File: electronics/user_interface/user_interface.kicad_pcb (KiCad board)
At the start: 2 copper layers, 100 x 100 mm, 66 parts, among them J1 Conn_01x06, J2 Conn_02x05_Odd_Even, SW1 ALPS_EC11E18244A5, U1 PCF8574, U2 PCF8574

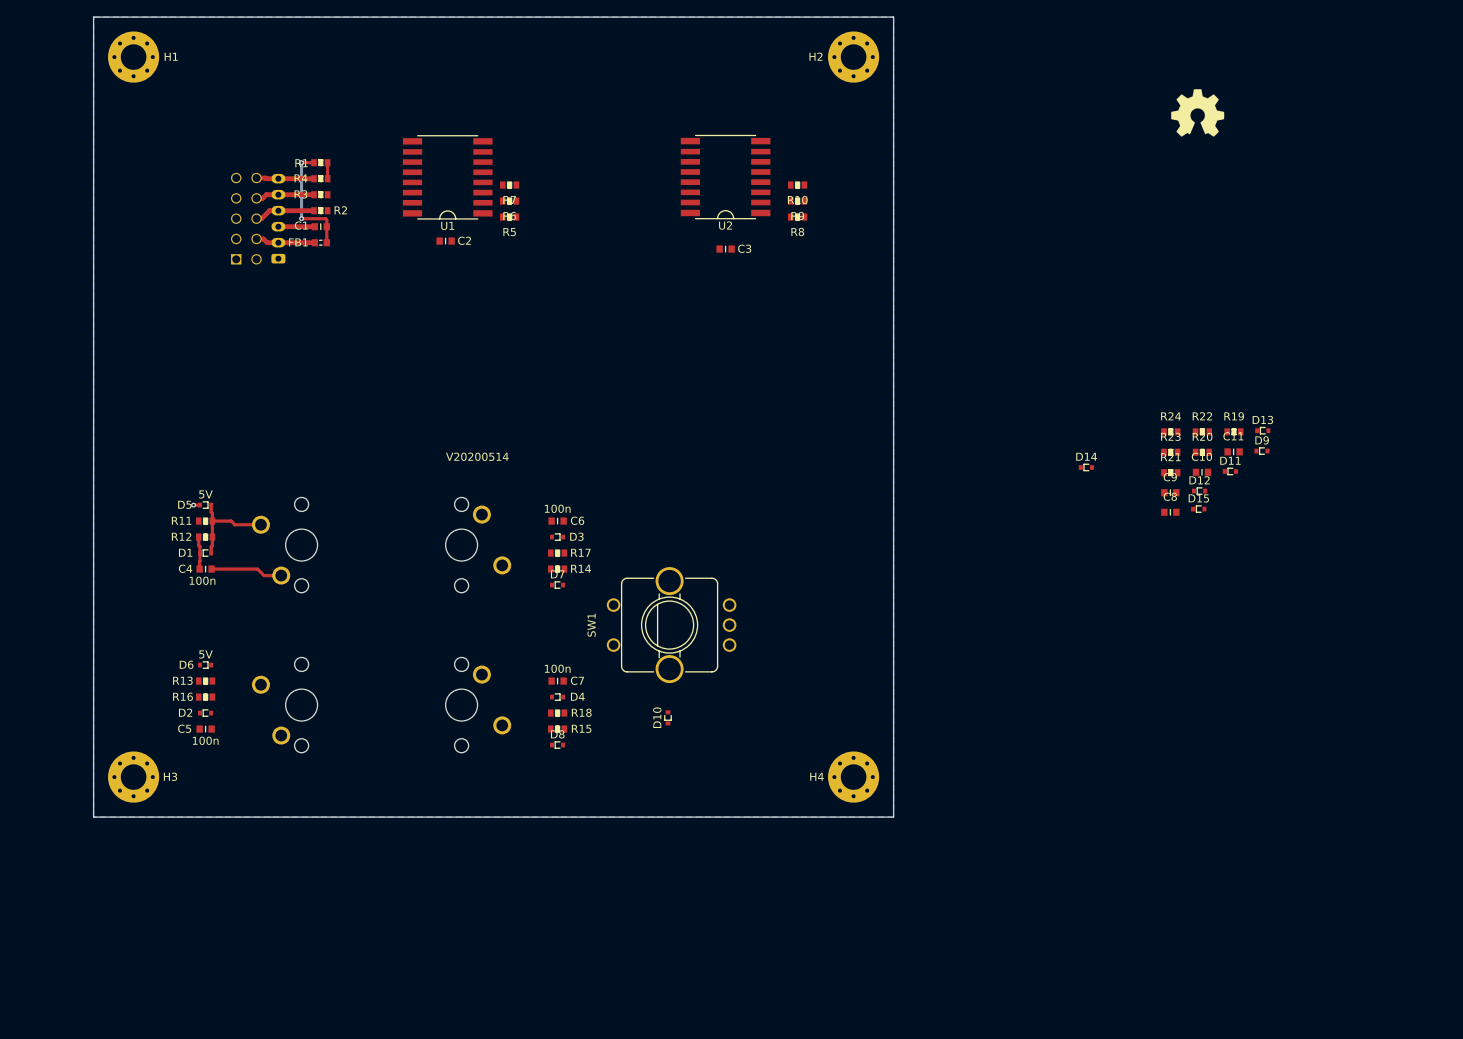
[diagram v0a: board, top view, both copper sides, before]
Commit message: imported LCD parts, changed board size
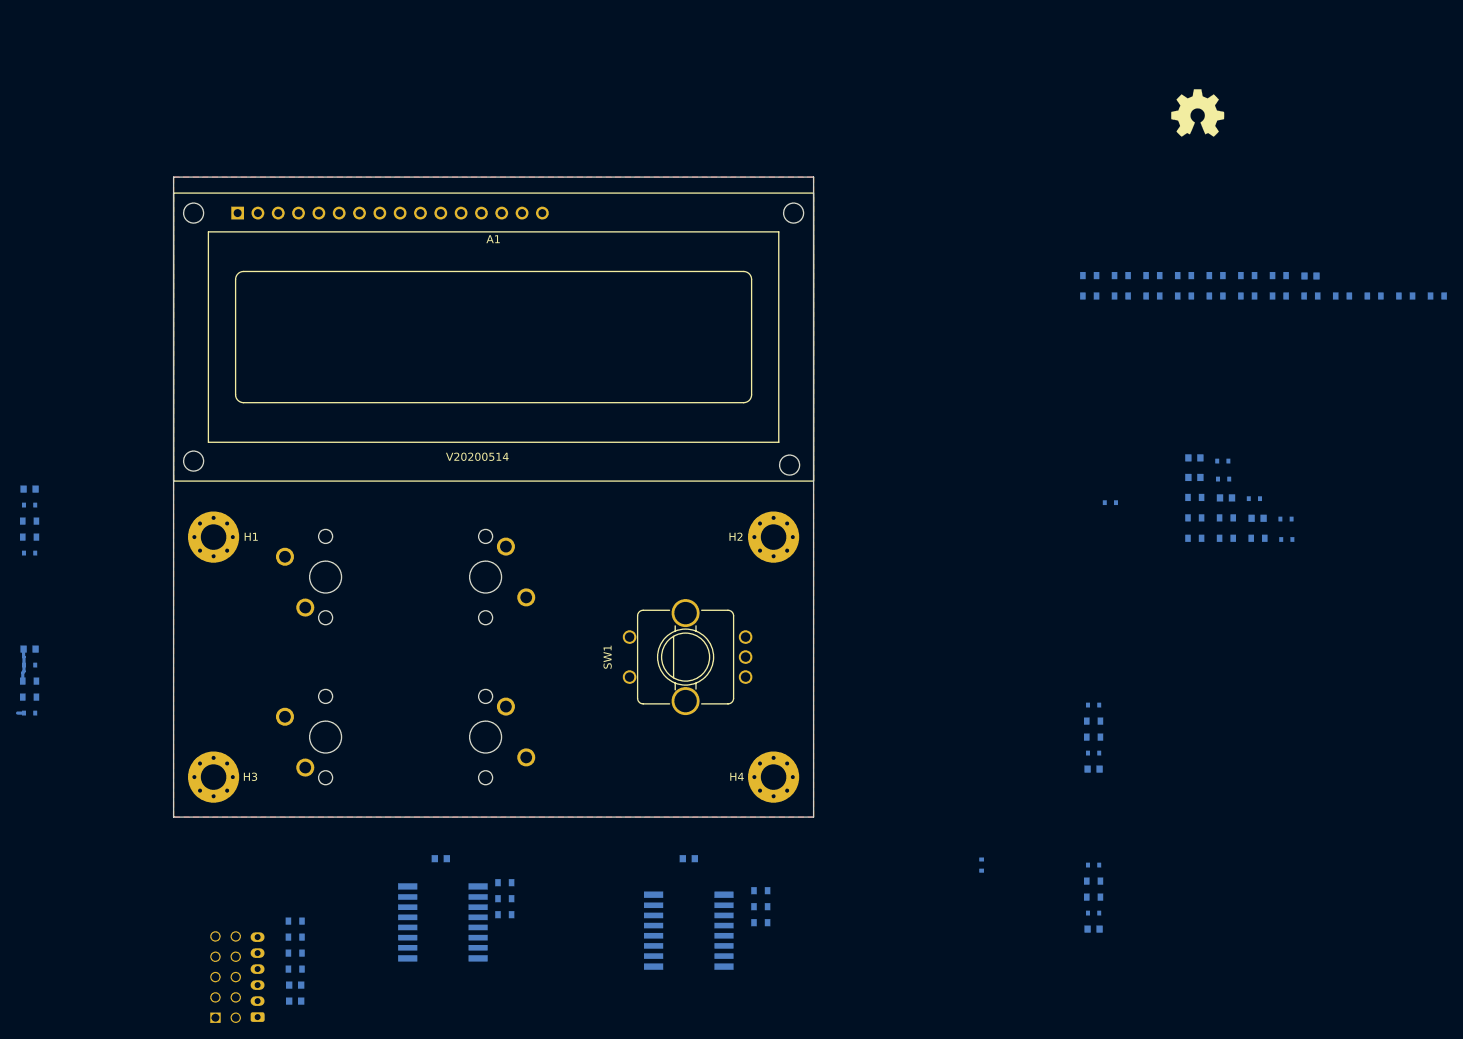
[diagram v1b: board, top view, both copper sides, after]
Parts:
- added A1: LCM1602, SquantorModules:LCM1602K, F.Cu at (150.0, 90.0)
- added C12: 1u, SquantorRcl:C_0603, B.Cu at (252.1, 82.4)
- added R25: 4.7K, SquantorRcl:R_0603_hand, B.Cu at (228.5, 84.9)
- added R26: 4.7K, SquantorRcl:R_0603_hand, B.Cu at (232.4, 84.9)
- added R27: 4.7K, SquantorRcl:R_0603_hand, B.Cu at (236.4, 84.9)
- added R28: 4.7K, SquantorRcl:R_0603_hand, B.Cu at (240.3, 84.9)
- added R29: 4.7K, SquantorRcl:R_0603_hand, B.Cu at (244.3, 84.9)
- added R30: 4.7K, SquantorRcl:R_0603_hand, B.Cu at (248.2, 84.9)
- added R31: 4.7K, SquantorRcl:R_0603_hand, B.Cu at (252.2, 84.9)
- added R32: 4.7K, SquantorRcl:R_0603_hand, B.Cu at (256.1, 84.9)
- added R33: 4.7K, SquantorRcl:R_0603_hand, B.Cu at (248.2, 82.3)
- added R34: 4.7K, SquantorRcl:R_0603_hand, B.Cu at (260.1, 84.9)
- added R35: 4.7K, SquantorRcl:R_0603_hand, B.Cu at (264.0, 84.9)
- added R36: 4.7K, SquantorRcl:R_0603_hand, B.Cu at (268.0, 84.9)
- added R37: 4.7K, SquantorRcl:R_0603_hand, B.Cu at (224.5, 82.3)
- added R38: TBD, SquantorRcl:R_0603_hand, B.Cu at (228.5, 82.3)
- added R39: 0, SquantorRcl:R_0603_hand, B.Cu at (232.4, 82.3)
- added R40: TBD, SquantorRcl:R_0603_hand, B.Cu at (236.4, 82.3)
- added R41: TBD, SquantorRcl:R_0603_hand, B.Cu at (240.3, 82.3)
- added R42: 0, SquantorRcl:R_0603_hand, B.Cu at (244.3, 82.3)
- added R43: NTC?, SquantorRcl:R_0603_hand, B.Cu at (224.5, 84.9)
- C1, C10, C11, C2, C3, C4, C5, C6, C7, C8, C9, D1, D10, D11, D12, D13, D14, D15, D2, D3, D4, D5, D6, D7, D8, D9, FB1, R1, R10, R11, R12, R13, R14, R15, R16, R17, R18, R19, R2, R20, R21, R22, R23, R24, R3, R4, R5, R6, R7, R8, R9, U1, U2: moved to B.Cu
- moved C1 94.9 mm to (125.2, 171.0)
- moved FB1 94.9 mm to (125.2, 173.0)
- moved R1 94.9 mm to (125.2, 163.0)
- moved R2 94.9 mm to (125.2, 169.0)
- moved R3 94.9 mm to (125.2, 167.0)
- moved R4 94.9 mm to (125.2, 165.0)
- moved J1 94.8 mm to (120.5, 175.0)
- moved J2 94.8 mm to (116.5, 170.0)
- moved U2 94.3 mm to (174.4, 164.2)
- moved U1 93.1 mm to (143.7, 163.2)
- moved R10 92.3 mm to (183.4, 163.2)
- moved R7 91.2 mm to (151.4, 162.2)
- moved R9 88.3 mm to (183.4, 161.2)
- moved R6 87.2 mm to (151.4, 160.2)
- moved R8 84.3 mm to (183.4, 159.2)
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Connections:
- U1 pad 10: Net-(U1-Pad10) -> /RW
- U1 pad 11: Net-(U1-Pad11) -> /RS
- U1 pad 4: Net-(U1-Pad4) -> /DB0
- U1 pad 5: Net-(U1-Pad5) -> /DB1
- U1 pad 6: Net-(U1-Pad6) -> /DB2
- U1 pad 7: Net-(U1-Pad7) -> /DB3
- U1 pad 9: Net-(U1-Pad9) -> /E
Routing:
- net /VDD: track 14.6 -> 0.00 mm, vias 2 -> 0
- net /VSS: track 14.4 -> 0.80 mm, vias 1 -> 0
- net Net-(D1-Pad2): track 12.4 -> 0.00 mm
- net /SDA_RAW: track 7.59 -> 0.00 mm
- net /VDD_RAW: track 7.47 -> 0.00 mm
- net /SCL_RAW: track 7.37 -> 0.00 mm
- net /!INT_RAW: track 7.21 -> 0.00 mm
- net /!INT: track 2.00 -> 0.00 mm
- added copper zone on F.Cu, net /VSS
- removed copper zone on B.Cu, net /VSS
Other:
- board size 100 x 100 mm -> 80 x 80 mm

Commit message: beautified schematic a bit, passes ERC
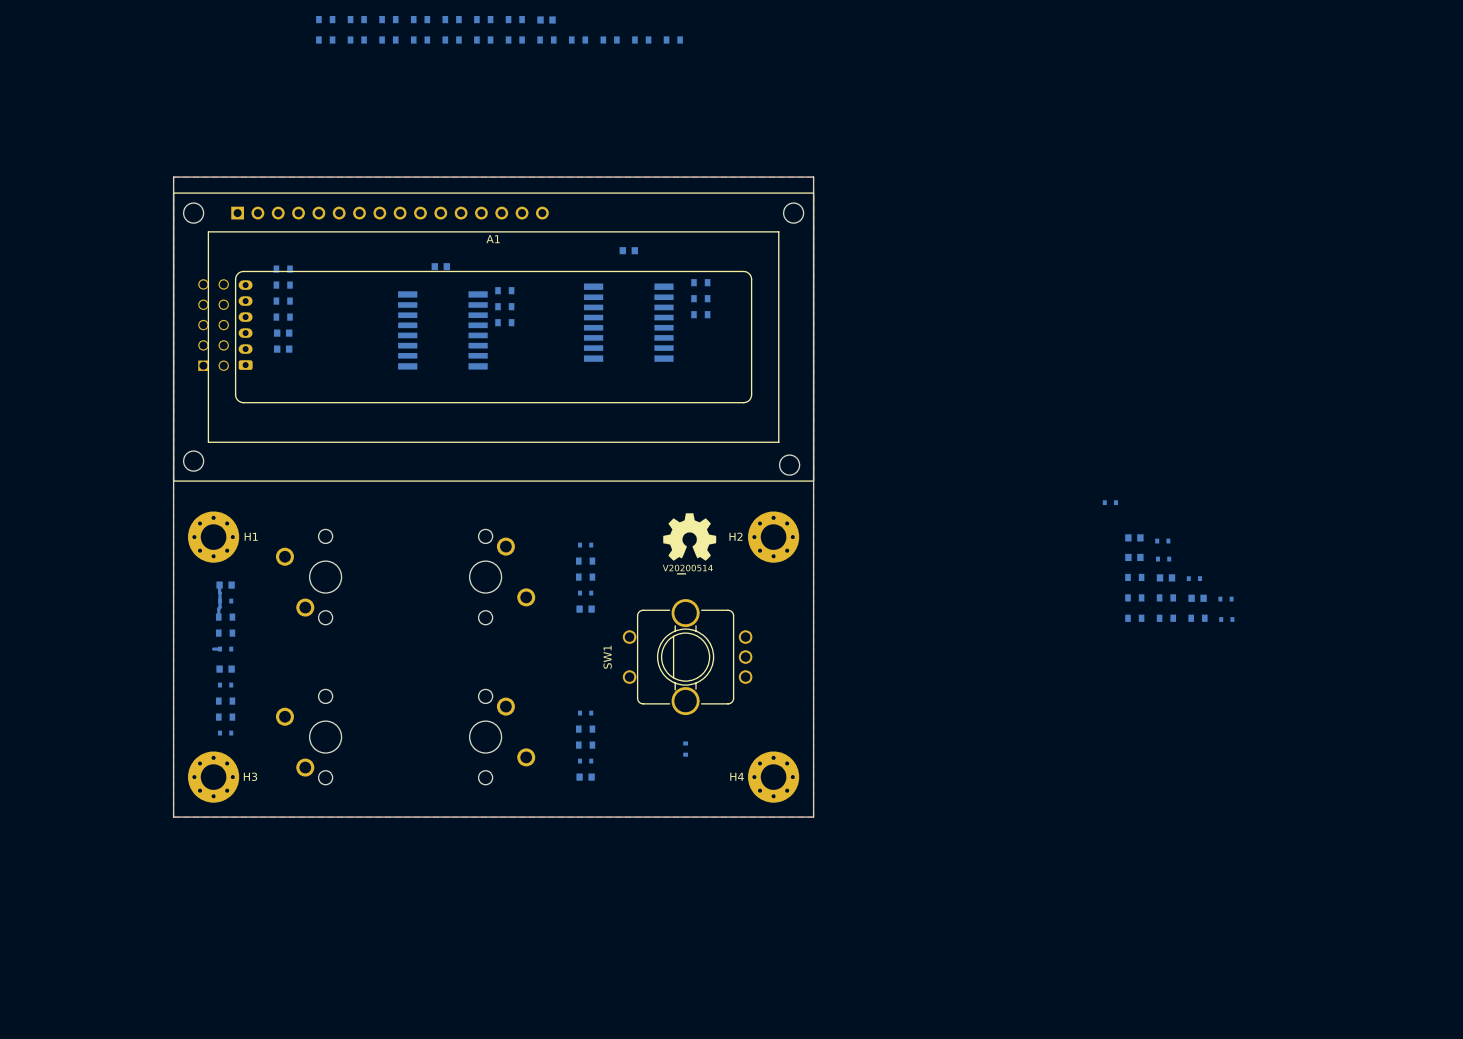
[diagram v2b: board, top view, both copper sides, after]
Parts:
- N2: footprint SquantorLabels:Label_version -> SquantorLabels:Label_Generic
- moved C12 100.7 mm to (156.6, 50.4)
- moved R25 100.7 mm to (133.0, 52.9)
- moved R26 100.7 mm to (136.9, 52.9)
- moved R27 100.7 mm to (140.9, 52.9)
- moved R28 100.7 mm to (144.8, 52.9)
- moved R29 100.7 mm to (148.8, 52.9)
- moved R30 100.7 mm to (152.7, 52.9)
- moved R31 100.7 mm to (156.7, 52.9)
- moved R32 100.7 mm to (160.6, 52.9)
- moved R33 100.7 mm to (152.7, 50.3)
- moved R34 100.7 mm to (164.6, 52.9)
- moved R35 100.7 mm to (168.5, 52.9)
- moved R37 100.7 mm to (129.0, 50.3)
- moved R38 100.7 mm to (133.0, 50.3)
- moved R39 100.7 mm to (136.9, 50.3)
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
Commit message: mechanical components placed, initial placing of passives
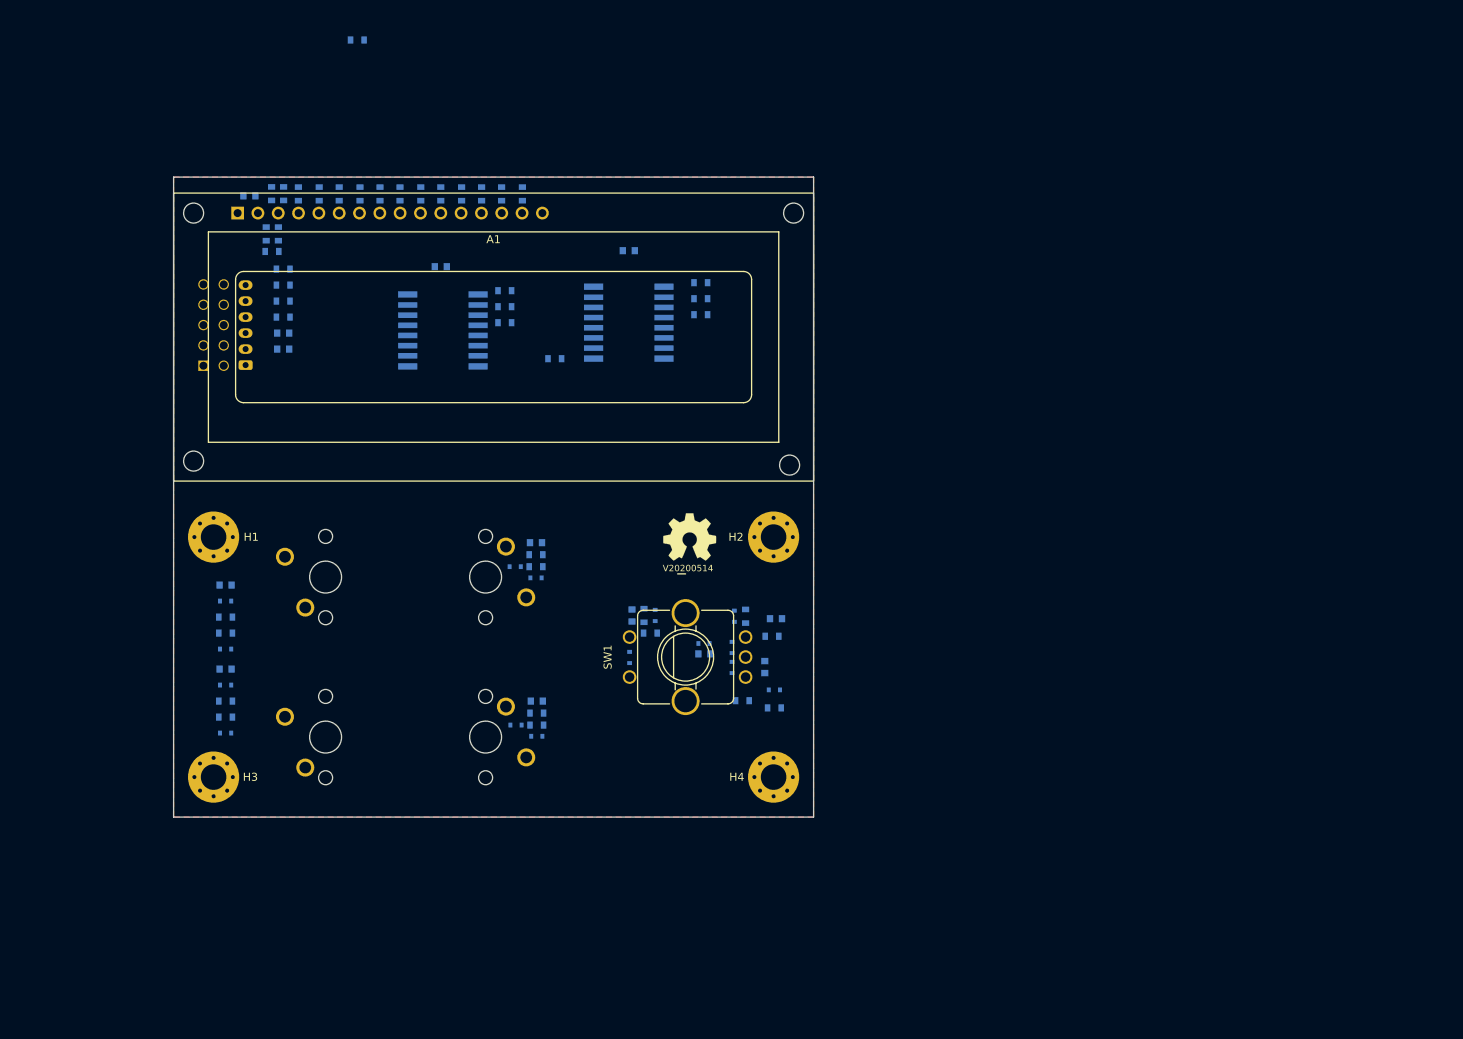
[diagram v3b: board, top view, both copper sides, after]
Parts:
- moved D9 74.9 mm to (167.0, 130.1), turned to 270 degrees
- moved R19 68.5 mm to (169.6, 127.0)
- moved R22 65.3 mm to (168.8, 124.8), turned to 270 degrees
- moved D12 63.9 mm to (170.2, 124.8), turned to 270 degrees
- moved C8 63.5 mm to (167.3, 124.8), turned to 270 degrees
- moved C11 62.0 mm to (176.3, 129.6), turned to 180 degrees
- moved D15 58.8 mm to (176.3, 128.3)
- moved D11 58.4 mm to (179.8, 128.8), turned to 270 degrees
- moved D13 57.2 mm to (185.1, 134.1)
- moved R20 50.9 mm to (185.1, 136.3)
- moved R23 50.7 mm to (181.1, 135.4)
- moved D14 49.1 mm to (180.1, 124.9), turned to 270 degrees
- moved C10 49.0 mm to (185.3, 125.2)
- moved R24 48.7 mm to (181.5, 124.9), turned to 270 degrees
- moved C9 48.2 mm to (183.9, 131.2), turned to 90 degrees
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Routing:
- net /Button_00: track 4.08 -> 0.00 mm
- net /VSS: track 0.80 -> 0.00 mm

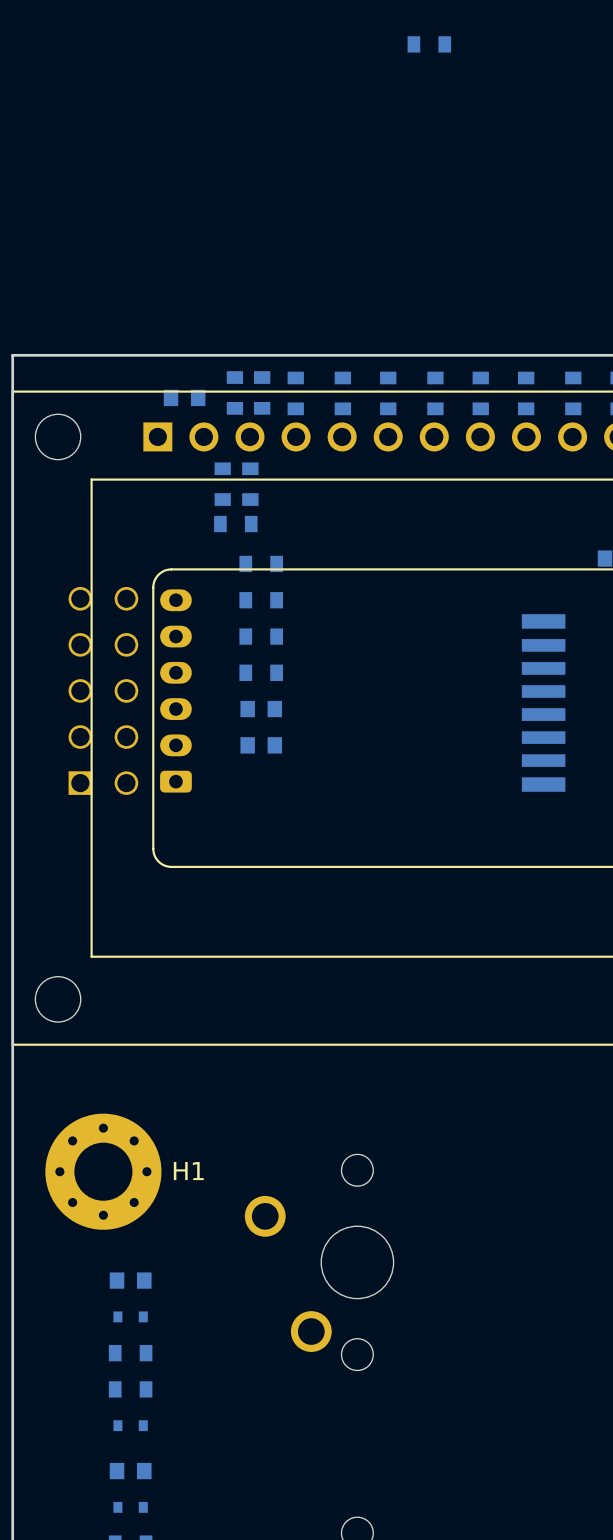
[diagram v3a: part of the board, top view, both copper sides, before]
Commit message: component placement
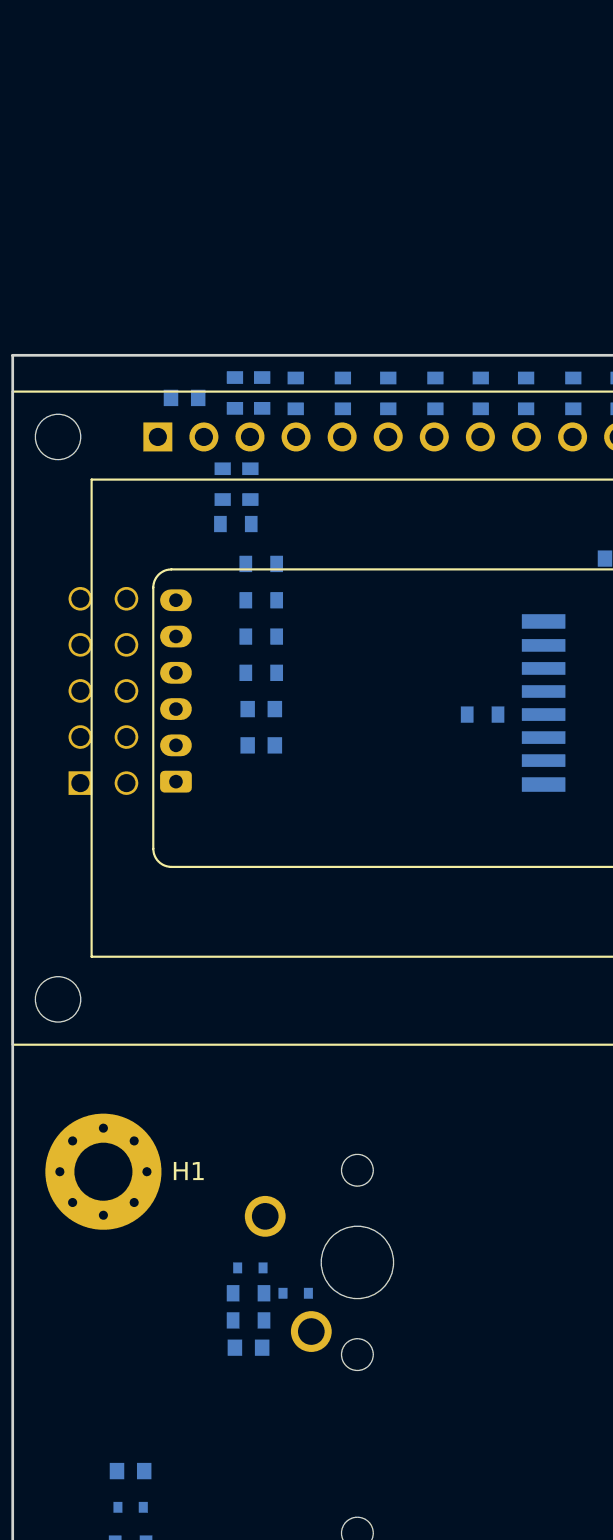
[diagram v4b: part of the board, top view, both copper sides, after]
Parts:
- moved R25 37.1 mm to (135.9, 89.8)
- moved D5 11.7 mm to (125.6, 121.7), turned to 0 degrees
- moved R11 7.53 mm to (123.0, 123.2)
- moved C4 7.48 mm to (123.0, 124.7)
- moved R12 7.29 mm to (123.0, 121.7)
- moved D1 7.13 mm to (123.1, 120.3)
